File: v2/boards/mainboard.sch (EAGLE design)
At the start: 163 parts, among them IC1 LM2596S-ADJ, IC10 PCF8574P, IC11 UDN2981A, IC13 PAM8403, IC2 LM2596S-5.0, IC3 LD1117A, IC4 LM393, IC5 MCP101-300, IC6 TSOP34830, IC7 DRV8835, IC8 TEENSY 3.6, IC9 PCA9634, J1 Bat_In, J10 SPI_2, J11 I2C_0, J12 I2C_1, J13 I2C_3, J133 USB_Host, J14 BNO055, J15 Uart_2, J16 Uart_5, J17 Uart_6 (LP), J18 BPS, J19 Servo_2, J2 Erw_Pow, J20 Servo_3, J21 Erw_Servo, J22 Erw_PWM, J23 ESP01 Prog, J24 SWD, J25 SWD_KL02, J26 SWD_KL02, J27 SPEAKER_L, J28 SPEAKER_R, J29 AUDIO_TEENSY, J3 Servo_1, J30 Erw_ENA, J31 Erw_GPIO, J32 Erw_analog, J4 H-Bridge Mode, J5 I2C0_5V, J6 SPI_0, J7 SPI_0, J8 SPI_0, J9 SPI_2, SW1 TL32PO, U1 IRL3103, U2 BS108, U3 BS108, U4 BS108, U5 BS108, U6 BS108, U7 BS108, X1 max. 18V

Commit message: ct-bot v2 schematic updated
 - use of i2c sensors
 - adjustable luminosity for CNY70 sensors
 - ENA driver circuit updated for low-side switching
 - ESP32 for Wi-Fi, SWD, RC5 decoding
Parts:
- removed C32: 100nF, rcl:C-EU025-025X050
- removed ESP-12: ESP-12, adafruit:ESP-12
- removed J133: USB_Host, ct-bot:PINHD-1X4
- removed U2, U3: BS108, ct-bot:BS108
- added C29: 470uF, rcl:CPOL-EUE3.5-8
- added D5, D6, D7, D8, D9: 1N4148, ct-bot:1N41480207/2V
- added IC12: ESP-WROOM-32, ct-bot:ESP-WROOM-32
- added J33: Erw_analog, ct-bot:PINHD-1X2
- added J34: USB_Host, ct-bot:PINHD-1X4
- added R53, R54: 4k7, rcl:R-EU_0204/2V
- added R55, R56: 10k, rcl:R-EU_0204/2V
- added R57: 5k, ct-bot:R-TRIMM64W
- added R58: ?, rcl:R-EU_0204/2V
- added R59: ?, rcl:R-EU_0204/7
- added U8, U9: BS108, ct-bot:BS108
- C17: value 220uF -> 100nF; device rcl:CPOL-EUE2-5 -> rcl:C-EU025-025X050
- C18: value 100nF -> 220uF; device rcl:C-EU025-025X050 -> rcl:CPOL-EUE2-5
- C20: value 100uF -> 100nF; device rcl:CPOL-EUE2-5 -> rcl:C-EU025-025X050
- C22: value 470nF -> 10uF
- C23, C27: value 1uF -> 470nF
- C25: value 100nF -> 1uF
- C26: value 470nF -> 100nF
- C28: value 470uF -> 1uF; device rcl:CPOL-EUE3.5-8 -> rcl:C-EU025-025X050
- IC10: value PCF8574P -> TSOP34830; device ct-bot:PCF8574P -> ct-bot:TSOP34830
- IC11: value UDN2981A -> DRV8835; device ct-bot:UDN2981A -> ct-bot:DRV8835THROUGHHOLE
- IC6: value TSOP34830 -> TEENSY 3.6; device ct-bot:TSOP34830 -> ct-bot:TEENSY3_6
- IC7: value DRV8835 -> PCA9634; device ct-bot:DRV8835THROUGHHOLE -> ct-bot:PCA9634-SO20
- IC8: value TEENSY 3.6 -> PCA9672; device ct-bot:TEENSY3_6 -> ct-bot:PCA9672D
- J10, J9: value SPI_2 -> SPI_0
- J11: value I2C_0 -> SPI_2; device ct-bot:PINHD-1X4 -> ct-bot:PINHD-1X7
- J12: value I2C_1 -> SPI_2; device ct-bot:PINHD-1X4 -> ct-bot:PINHD-1X6
- J13: value I2C_3 -> I2C_0
- J14: value BNO055 -> I2C_1; device ct-bot:PINHD-1X6 -> ct-bot:PINHD-1X4
- J15: value Uart_2 -> I2C_3
- J16: value Uart_5 -> BNO055; device ct-bot:PINHD-1X4 -> ct-bot:PINHD-1X6
- J17: value Uart_6 (LP) -> Uart_2
- J18: value BPS -> Uart_5; device ct-bot:PINHD-1X3 -> ct-bot:PINHD-1X4
- J19: value Servo_2 -> Uart_6 (LP)
- J20: value Servo_3 -> BPS; device ct-bot:PINHD-1X4 -> ct-bot:PINHD-1X3
- J21: value Erw_Servo -> Servo_2; device ct-bot:PINHD-1X2 -> ct-bot:PINHD-1X4
- J22: value Erw_PWM -> Servo_3; device ct-bot:PINHD-1X6 -> ct-bot:PINHD-1X4
- J23: value ESP01 Prog -> Erw_Servo; device ct-bot:PINHD-1X4 -> ct-bot:PINHD-1X2
- J24: value SWD -> Erw_PWM
- J25: value SWD_KL02 -> ESP32_PROG; device ct-bot:PINHD90-1X2/90 -> ct-bot:PINHD-1X3
- J26: value SWD_KL02 -> SPEAKER_L
- J27: value SPEAKER_L -> SPEAKER_R
- J28: value SPEAKER_R -> AUDIO_TEENSY; device ct-bot:PINHD-1X2 -> ct-bot:PINHD-1X3
- J29: value AUDIO_TEENSY -> SWD; device ct-bot:PINHD-1X3 -> ct-bot:PINHD-1X6
- J3: value Servo_1 -> I2C0_5V
- J30: value Erw_ENA -> SWD_KL02; device pinhead:PINHD-2X4 -> ct-bot:PINHD90-1X2/90
- J31: value Erw_GPIO -> Erw_ENA; device ct-bot:PINHD-1X2 -> ct-bot:PINHD-1X3
- J32: value Erw_analog -> Erw_GPIO
- J4: value H-Bridge Mode -> I2C3_5V; device ct-bot:PINHD-1X2 -> ct-bot:PINHD-1X4
- J5: value I2C0_5V -> Servo_1
- J6: value SPI_0 -> H-Bridge Mode; device con-harting-ml:ML10 -> ct-bot:PINHD-1X2
- J7: value SPI_0 -> RC5_SEL; device ct-bot:PINHD-1X7 -> ct-bot:PINHD-1X3
- J8: device ct-bot:PINHD-1X6 -> con-harting-ml:ML10
- LDR1, LDR2: value MPY54C569 -> (none)
- R10, R11: value 47k -> 180
- R12, R13: value 210 -> 47k
- R27, R28, R29, R30, R31: device rcl:R-EU_0204/2V -> rcl:R-EU_0204/7
- R32: value 470k -> 100
- R34: value 4k7 -> 470k
- R35: value 100 -> 4k7
- R37: value 3k9 -> 10k
- R38: value 220 -> 10k
- R39: value 590 -> 1k1
- R40: value 115 -> 1k1
- R42, R48: value 4k7 -> 1k8
- R44: value 4k7 -> 3k9
- R45: value 4k7 -> 220
- R46: value 10k -> 590
- R47: value 10k -> 115
- R50: value 5k -> 4k7; device ct-bot:R-TRIMM64W -> rcl:R-EU_0204/2V
- R51: value ? -> 10k
- R52: value ? -> 4k7
- ST3: device ct-bot:PS25-5PS25-5 -> ct-bot:PS25-6
- U1: device transistor-power:IRF740 -> ct-bot:IRF740
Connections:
- removed net ABST_SHUT_L: IC10.P3, U2.G
- removed net ABST_SHUT_R: IC10.P4, U3.G
- removed net DRV_ERW_3: IC11.O7, J30.6
- removed net DRV_ERW_4: IC11.O8, J30.8
- removed net DRV_KANTLED: IC11.O2, R14.2, R15.1
- removed net DRV_LINIE: IC11.O3, R18.2, R19.2
- removed net DRV_RADLED: IC11.O1, R12.2, R13.1
- removed net DRV_SCHRANKE: IC11.O4, ST1.9
- removed net ENA_ERW_2: IC10.P7, IC11.I6, J30.3
- removed net ENA_ERW_3: IC11.I8, J30.5
- removed net ENA_ERW_4: IC11.I7, J30.7
- removed net ENA_KANTLED: IC10.P1, IC11.I2
- removed net ENA_LINIE: IC10.P2, IC11.I3
- removed net ENA_RADLED: IC10.P0, IC11.I1
- removed net ENA_SCHRANKE: IC10.P5, IC11.I4
- removed net N$12: ESP-12.GPIO15, J23.3
- removed net N$14: ESP-12.GPIO0, J23.2
- new net ABST_SHDN_L: D5.C, IC8.P0
- new net ABST_SHDN_R: D6.C, IC8.P1
- new net BNO055_RESET: IC8.P3, J16.6
- new net DRV_KANTLED_L: IC9.LED2, R11.2
- new net DRV_KANTLED_R: IC9.LED3, R15.1
- new net DRV_LINE_L: IC9.LED4, R19.2
- new net DRV_LINE_R: IC9.LED5, R18.2
- new net DRV_RADLED_L: IC9.LED0, R10.2
- new net DRV_RADLED_R: IC9.LED1, R14.1
- new net EN: D8.A, IC12.EN, R56.1
- new net ENA_AUDIO: IC13.SHND, IC8.P4
- new net ESP32_PROG: D9.C, IC8.P6
- new net ESP32_RESET: D8.C, IC8.P5
- new net GPIO_28: IC6.28/ALT-MOSI0, J7.3
- new net IO0: D9.A, IC12.IO0, R55.2
- new net IO10: IC12.SD3
- new net IO11: IC12.CMD
- new net IO13: IC12.IO13
- new net IO15: IC12.IO15
- new net IO18: IC12.IO18
- new net IO19: IC12.IO19
- new net IO21: IC12.IO21
- new net IO34: IC12.IO34
- new net IO35: IC12.IO35
- new net IO36: IC12.SENSOR_VP
- new net IO39: IC12.SENSOR_VN
- new net IO4: IC12.IO4
- new net IO5: IC12.IO5
- new net IO6: IC12.CLK
- new net IO7: IC12.SDO
- new net IO8: IC12.SD1
- new net IO9: IC12.SD2
- new net N$49: IC8.!RESET, R51.1
- new net RC5_ESP32: IC12.IO23, J7.1
- new net RXD0: IC12.RXD0, J25.3
- new net SCHRANKE_SHDN: D7.C, IC8.P2
- new net SCL3_5V: IC7.SCL, IC8.SCL, IC9.SCL, J4.4, R42.1, U8.D
- new net SDA3_5V: IC7.SDA, IC8.SDA, IC9.SDA, J4.3, R41.1, U9.D
- new net TXD0: IC12.TXD0, J25.2
- new net VL6180X_SHDN: D7.A, ST1.5
- net +3V3: now also C22.1, IC10.VS, IC12.3V3, J20.3, J8.10, R12.2, R13.1, R36.2, R39.2, R40.2, R52.2, R53.2, R54.2, R55.1, R56.2, U8.G, U9.G; no longer C21.1, ESP-12.CH_PD, ESP-12.VCC, IC6.VS, J18.3, J23.1, J6.10, R10.2, R11.1, R44.2, R45.2, R48.2, R49.2
- net +5V: now also C17.1, C18.+, C20.1, C21.1, C25.1, C28.1, C29.+, IC11.VCC, IC6.VIN, IC7.A0, IC7.A2, IC7.A4, IC7.VDD, IC8.VDD, IC9.A3, J10.1, J14.2, J16.1, J18.2, J19.2, J3.2, J34.1, J4.2, J9.1, R37.2, R38.2, R41.2, R42.2, R44.1, R45.1, R46.1, R47.1, R48.1, R49.1, R50.1, R51.2, ST1.1, ST2.1, ST3.1; no longer C16.1, C17.+, C18.1, C20.+, C23.1, C27.1, C28.+, IC10.A0, IC10.VDD, IC11.VS, IC7.VCC, IC8.VIN, J10.2, J133.1, J14.1, J16.2, J4.1, J5.2, J7.1, J9.2, R36.1, R37.1, R38.1, R39.1, R40.1, R41.1, R42.1, R46.2, R47.2, ST1.3, ST2.3
- net +6V: now also IC11.VIN, J21.2, J22.2, J5.2; no longer IC7.VIN, J19.2, J20.2, J3.2
- net 3V3_TEENSY: now also C16.1, IC6.3V3, J29.1; no longer C32.1, IC8.3V3, J24.1
- net A22_DAC1: now also IC6.DAC1, J33.1; no longer IC8.DAC1, J32.1
- net AUDIO_OUT: now also IC6.DAC0, J28.1, J33.2; no longer IC8.DAC0, J29.1, J32.2
- net BAT_IN_FB: now also IC6.39/A20/ALT-MISO0; no longer IC8.39/A20/ALT-MISO0
- net BPS: now also IC6.42, J20.1; no longer IC8.42, J18.1
- net DRV_ERW_1: now also IC9.LED6, J31.2; no longer IC11.O5, J30.2
- net DRV_ERW_2: now also IC9.LED7, J31.3; no longer IC11.O6, J30.4
- net ENA_ERW_1: now also IC8.P7, J31.1; no longer IC10.P6, IC11.I5, J30.1
- net ENC_L: now also ST1.8; no longer ST1.1
- net ENC_R: now also ST2.8; no longer ST2.1
- net FERNBED: now also IC10.OUT, J7.2; no longer IC6.OUT, IC8.28/ALT-MOSI0
- net GND: now also C17.2, C18.-, C20.2, C22.2, C26.2, C28.2, C29.-, IC10.GND, IC11.LGND, IC11.MGND, IC12.GND@1, IC12.GND@15, IC12.GND@38, IC12.IO2, IC6.AGND, IC7.A1, IC7.A3, IC7.A5, IC7.A6, IC7.OE, IC7.VSS, IC8.AD0, IC8.AD1, IC8.VSS, J10.2, J14.1, J16.3, J18.1, J20.2, J21.1, J22.1, J25.1, J29.3, J34.4, J4.1, J9.2, R57.E, ST3.6; no longer C17.-, C18.2, C20.-, C23.2, C27.2, C28.-, C32.2, ESP-12.GND, IC10.A1, IC10.A2, IC10.VSS, IC11.GND, IC7.LGND, IC7.MGND, IC8.AGND, IC8.GND, IC9.A3, J10.1, J133.4, J14.3, J16.1, J18.2, J20.1, J23.4, J24.3, J6.2, J7.2, J9.1, R50.E, ST3.5, U2.S, U3.S
- net GPIO_24: now also IC6.24, J32.1; no longer IC8.24, J31.1
- net GPIO_46: now also IC6.46/SCK2, J32.2; no longer IC8.46/SCK2, J31.2
- net KANTE_L: now also IC6.18/A4/PWM/T/SDA0, R12.1, ST1.9; no longer IC8.18/A4/PWM/T/SDA0, R10.1, ST1.6
- net KANTE_R: now also IC6.19/A5/PWM/T/SCL0, R13.2, ST2.9; no longer IC8.19/A5/PWM/T/SCL0, R11.2, ST2.6
- net KL02_DC: now also IC12.IO12, J30.1; no longer J25.1, J26.1
- net KL02_DD: now also IC12.IO14, J30.2; no longer J25.2, J26.2
- net LDR_L: now also IC6.49/A23, R33.1; no longer IC8.49/A23, R32.1
- net LDR_R: now also IC6.50/A24, R34.1; no longer IC8.50/A24, R33.1
- net LINE_IN_L: now also J28.2, R57.A; no longer J29.2, R50.A
- net LINE_IN_R: now also C27.2, J28.3; no longer C26.2, J29.3
- net LINIE_L: now also IC6.A10, ST3.4; no longer IC8.A10, ST3.3
- net LINIE_R: now also IC6.A11, ST3.5; no longer IC8.A11, ST3.4
- net MOT_L_1: now also IC11.AOUT1; no longer IC7.AOUT1
- net MOT_L_2: now also IC11.AOUT2; no longer IC7.AOUT2
- net MOT_L_DIR: now also IC11.APHASE, IC6.40; no longer IC7.APHASE, IC8.40
- net MOT_L_PWM: now also IC11.AENBL, IC6.35/A16/PWM; no longer IC7.AENBL, IC8.35/A16/PWM
- net MOT_R_1: now also IC11.BOUT1; no longer IC7.BOUT1
- net MOT_R_2: now also IC11.BOUT2; no longer IC7.BOUT2
- net MOT_R_DIR: now also IC11.BPHASE, IC6.41; no longer IC7.BPHASE, IC8.41
- net MOT_R_PWM: now also IC11.BENBL, IC6.36/A17/PWM; no longer IC7.BENBL, IC8.36/A17/PWM
- net N$1: now also ST3.3; no longer ST3.2
- net N$13: now also IC7.LED2; no longer IC9.LED2
- net N$15: now also IC7.LED3; no longer IC9.LED3
- net N$16: now also IC7.LED4; no longer IC9.LED4
- net N$17: now also IC7.LED5; no longer IC9.LED5
- net N$18: now also IC7.LED6; no longer IC9.LED6
- net N$19: now also IC7.LED7; no longer IC9.LED7
- net N$20: now also R43.2; no longer R36.2
- net N$21: now also R44.2; no longer R37.2
- net N$22: now also R45.2; no longer R38.2
- net N$23: now also R46.2; no longer R39.2
- net N$24: now also R47.2; no longer R40.2
- net N$25: now also R48.2; no longer R41.2
- net N$26: now also R49.2; no longer R42.2
- net N$27: now also R50.2; no longer R43.2
- net N$28: now also R32.1; no longer R35.1
- net N$3: now also IC11.MODE, J6.2; no longer IC7.MODE, J4.2
- net N$30: now also ST3.2; no longer ST3.1
- net N$31: now also J26.2; no longer J27.2
- net N$32: now also J26.1; no longer J27.1
- net N$33: now also C26.1; no longer C25.1
- net N$40: now also R58.1; no longer R51.1
- net N$41: now also C23.1, R58.2; no longer C22.1, R51.2
- net N$42: now also C23.2, R57.S; no longer C22.2, R50.S
- net N$43: now also J27.1; no longer J28.1
- net N$44: now also J27.2; no longer J28.2
- net N$45: now also R14.2, ST2.6; no longer R13.2, ST2.2
- net N$46: now also R59.1; no longer R52.1
- net N$47: now also R10.1, ST1.6; no longer R12.1, ST1.2
- net N$48: now also C27.1, R59.2; no longer C26.1, R52.2
- net N$51: now also R11.1, ST1.7; no longer R14.1, ST1.5
- net N$53: now also ST2.7; no longer ST2.5
- net N$6: now also IC7.LED0; no longer IC9.LED0
- net N$7: now also IC7.LED1; no longer IC9.LED1
- net PWM_ERW_1: now also IC6.16/A2/PWM/T/ALT-SCL0, J24.1; no longer IC8.16/A2/PWM/T/ALT-SCL0, J22.1
- net PWM_ERW_2: now also IC6.17/A3/PWM/T/ALT-SDA0, J24.2; no longer IC8.17/A3/PWM/T/ALT-SDA0, J22.2
- net PWM_ERW_3: now also IC6.30/PWM/T/ALT-CAN0RX, J24.3, J8.9; no longer IC8.30/PWM/T/ALT-CAN0RX, J22.3, J6.9
- net PWM_ERW_4: now also IC6.29/PWM/T/ALT-CAN0TX, J24.4; no longer IC8.29/PWM/T/ALT-CAN0TX, J22.4
- net PWM_ERW_5: now also IC6.4/PWM/SDA2/CAN0RX, J24.5; no longer IC8.4/PWM/SDA2/CAN0RX, J22.5
- net PWM_ERW_6: now also IC6.3/PWM/SCL2/CAN0TX, J24.6; no longer IC8.3/PWM/SCL2/CAN0TX, J22.6
- net RAD_L: now also IC6.43/CS2-0; no longer IC8.43/CS2-0
- net RAD_R: now also IC6.44/MOSI2; no longer IC8.44/MOSI2
- net RESET: now also IC12.IO22, IC6.RESET, J29.2; no longer IC8.RESET, J24.2
- net RX1: now also IC6.27/ALT-RX1/ALT-SCK0; no longer IC8.27/ALT-RX1/ALT-SCK0
- net RX2: now also IC6.9/PWM/RX2/CS0-1, J17.4; no longer IC8.9/PWM/RX2/CS0-1, J15.4
- net RX5: now also IC12.IO17, IC6.34/A15/CAN1RX/RX5/ALT-SDA0, J18.4; no longer ESP-12.TXD, IC8.34/A15/CAN1RX/RX5/ALT-SDA0, J16.4
- net RX6: now also IC6.47/SCL0/RX6, J19.4; no longer IC8.47/SCL0/RX6, J17.4
- net SCL0: now also IC6.7/PWM/RX3/ALT-SCL0/ALT-MOSI0, J13.4, R36.1; no longer IC10.SCL, IC8.7/PWM/RX3/ALT-SCL0/ALT-MOSI0, IC9.SCL, J11.4, R45.1
- net SCL0_5V: now also J16.5, J3.4, R38.1, ST1.3, ST2.3; no longer J14.5, J5.4, R47.1, ST1.8, ST2.8
- net SCL1: now also IC6.37/A18/PWM/SCL1, J14.4; no longer IC8.37/A18/PWM/SCL1, J12.4
- net SCL3: now also IC12.IO26, IC6.57/SCL3/PWM, J15.3, R40.1, U8.S; no longer IC8.57/SCL3/PWM, J13.3
- net SDA0: now also IC6.8/PWM/TX3/ALT-SDA0/ALT-MISO0, J13.3, R35.1; no longer IC10.SDA, IC8.8/PWM/TX3/ALT-SDA0/ALT-MISO0, IC9.SDA, J11.3, R44.1
- net SDA0_5V: now also J16.4, J3.3, R37.1, ST1.2, ST2.2; no longer J14.4, J5.3, R46.1, ST1.7, ST2.7
- net SDA1: now also IC6.38/A19/PWM/SDA1, J14.3; no longer IC8.38/A19/PWM/SDA1, J12.3
- net SDA3: now also IC12.IO25, IC6.56/SDA3/PWM, J15.4, R39.1, U9.S; no longer IC8.56/SDA3/PWM, J13.4
- net SERVO1_FB: now also IC6.22/A8/PWM/T, J5.4; no longer IC8.22/A8/PWM/T, J3.4
- net SERVO1_PWM: now also IC6.5/PWM/ALT-TX1/ALT-MISO1, J5.3, R52.1; no longer IC8.5/PWM/ALT-TX1/ALT-MISO1, J3.3, R34.1
- net SERVO2_FB: now also IC6.23/A9/PWM/T, J21.4; no longer IC8.23/A9/PWM/T, J19.4
- net SERVO2_PWM: now also IC6.6/PWM, J21.3, R53.1; no longer IC8.6/PWM, J19.3, R48.1
- net SERVO3_PWM: now also IC6.25, J22.3, R54.1; no longer IC8.25, J20.3, R49.1
- net SERVO4_PWM: now also IC6.20/A6/PWM/CS0-2/ALT-SCK1, J23.1, J9.6; no longer IC8.20/A6/PWM/CS0-2/ALT-SCK1, J21.1, J7.6
- net SERVO5_PWM: now also IC6.21/A7/PWM/CS0-3/ALT-MOSI1/ALT-RX1, J10.6, J23.2, J9.7; no longer IC8.21/A7/PWM/CS0-3/ALT-MOSI1/ALT-RX1, J21.2, J7.7, J8.6
- net SPI0_CS0: now also IC6.2/PWM, J8.6; no longer IC8.2/PWM, J6.6
- net SPI0_CS4: now also IC6.15/A1/CS0-4/T, J8.7; no longer IC8.15/A1/CS0-4/T, J6.7
- net SPI0_CS5: now also IC6.45/CS0-5/MISO2, J8.8; no longer IC8.45/CS0-5/MISO2, J6.8
- net SPI0_MISO: now also IC6.12/MISO0, J10.4, J9.4; no longer IC8.12/MISO0, J6.4, J7.4
- net SPI0_MOSI: now also IC6.11/MOSI0, J10.3, J9.3; no longer IC8.11/MOSI0, J6.3, J7.3
- net SPI0_SCK: now also IC6.14/A0/PWM/ALT-SCK0, J10.5, J9.5; no longer IC8.14/A0/PWM/ALT-SCK0, J6.5, J7.5
- net SPI1_CS0: now also IC6.31/A12/PWM/RX4/CS1-0; no longer IC8.31/A12/PWM/RX4/CS1-0
- net SPI1_MISO: now also IC6.1/TX1/MISO1/T; no longer IC8.1/TX1/MISO1/T
- net SPI1_MOSI: now also IC6.0/RX1/MOSI1/T; no longer IC8.0/RX1/MOSI1/T
- net SPI1_SCK: now also IC6.32/A13/PWM/TX4/SCK1; no longer IC8.32/A13/PWM/TX4/SCK1
- net SPI2_CS0: now also IC6.55, J11.6; no longer IC8.55, J9.6
- net SPI2_CS1: now also IC6.54/CS2-1, J11.7, J12.6; no longer IC8.54/CS2-1, J10.6, J9.7
- net SPI2_MISO: now also IC6.51/MISO2, J11.4, J12.4; no longer IC8.51/MISO2, J10.4, J9.4
- net SPI2_MOSI: now also IC6.52/MOSI2, J11.3, J12.3; no longer IC8.52/MOSI2, J10.3, J9.3
- net SPI2_SCK: now also IC6.53/PWM/SCK2, J11.5, J12.5; no longer IC8.53/PWM/SCK2, J10.5, J9.5
- net SWCLK: now also IC12.IO33, IC6.DC, J29.5; no longer IC8.DC, J24.5
- net SWDIO: now also IC12.IO32, IC6.DD, J29.6; no longer IC8.DD, J24.6
- net SWD_EN: now also IC12.IO27, IC6.DE, J29.4; no longer IC8.DE, J24.4
- net TEENSY_LED: now also IC6.13/LED/ALT-PWM/SCK0; no longer IC8.13/LED/ALT-PWM/SCK0
- net TX1: now also IC6.26/ALT-PWM/ALT-TX1/ALT-SCL2; no longer IC8.26/ALT-PWM/ALT-TX1/ALT-SCL2
- net TX2: now also IC6.10/PWM/TX2/CS0-0, J17.3; no longer IC8.10/PWM/TX2/CS0-0, J15.3
- net TX5: now also IC12.IO16, IC6.33/A14/CAN1TX/TX5/ALT-SCL0, J18.3; no longer ESP-12.RXD, IC8.33/A14/CAN1TX/TX5/ALT-SCL0, J16.3
- net TX6: now also IC6.48/SDA0/TX6, J19.3; no longer IC8.48/SDA0/TX6, J17.3
- net USB1_D+: now also IC6.D+, J34.3; no longer IC8.D+, J133.3
- net USB1_D-: now also IC6.D-, J34.2; no longer IC8.D-, J133.2
- net VBAT_RTC: now also IC6.VBAT; no longer IC8.VBAT
- net VL53L0X_SHUT_L: now also D5.A; no longer U2.D
- net VL53L0X_SHUT_R: now also D6.A; no longer U3.D
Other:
- note added: "Aktuatoren"
- note added: "ENA PWM"
- note added: "ENA digital"
- note added: "LDRs"
- note added: "LEDs"
- note added: "Power"
- note added: "RC5"
- note added: "Radencoder"
- note added: "Rev. 0.8.0"
- note added: "Sensoren"
- note added: "Teensy"
- note added: "ToDo: Signalauswahl"
- note added: "ToDo: testen"
- note removed: "/ MIC2981 / TBD62783A"
- note removed: "ESP12"
- note removed: "Rev. 0.7"
- note removed: "TODO: SWD-Pins verbinden an GPIOs? Widerstaende?"
- note removed: "ToDo: alternativ low-side switch (ULN 2803)?"
- note removed: "ToDo: testen! SHDN?"
- moved on the sheet: BT1, C10, C13, C16, C19, C22, C23, C24, C26, C27, IC13, IC5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

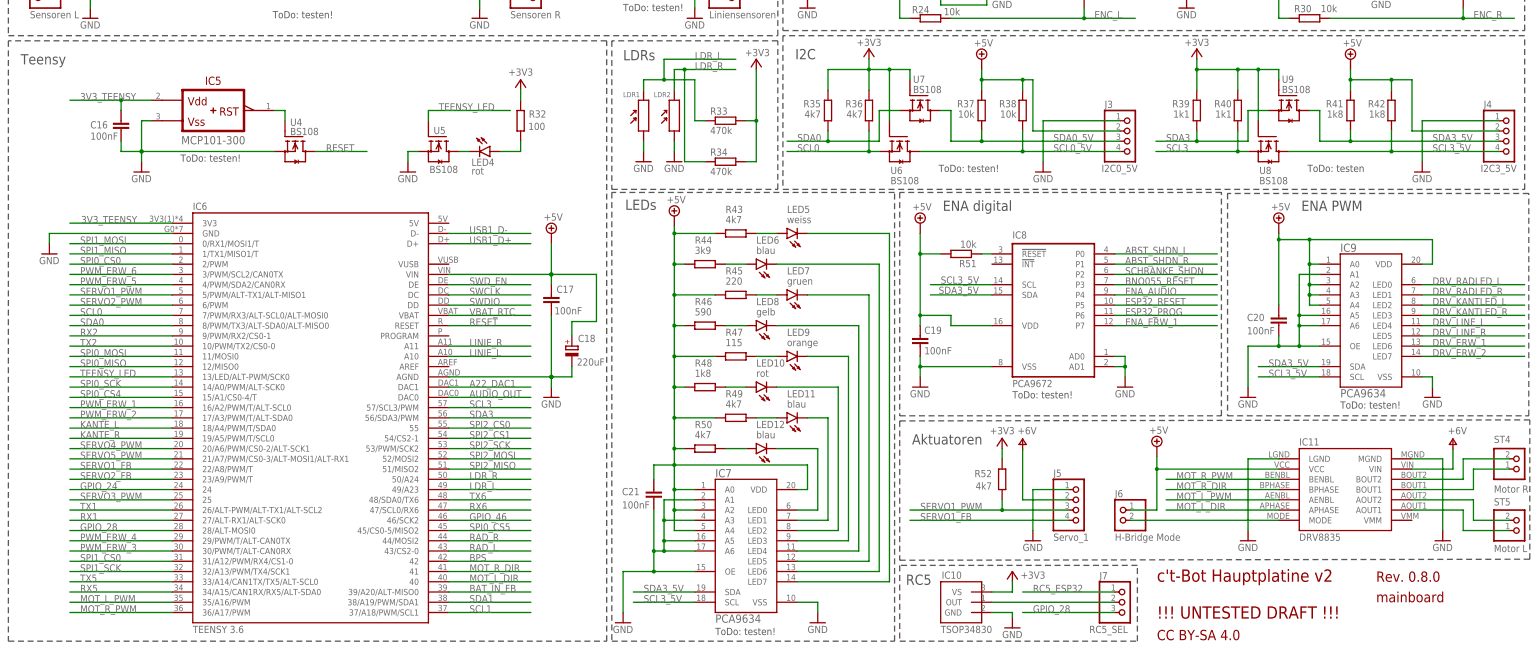
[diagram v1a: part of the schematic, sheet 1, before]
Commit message: PCA9672D (no longer manufactured) replaced with PCA9554D
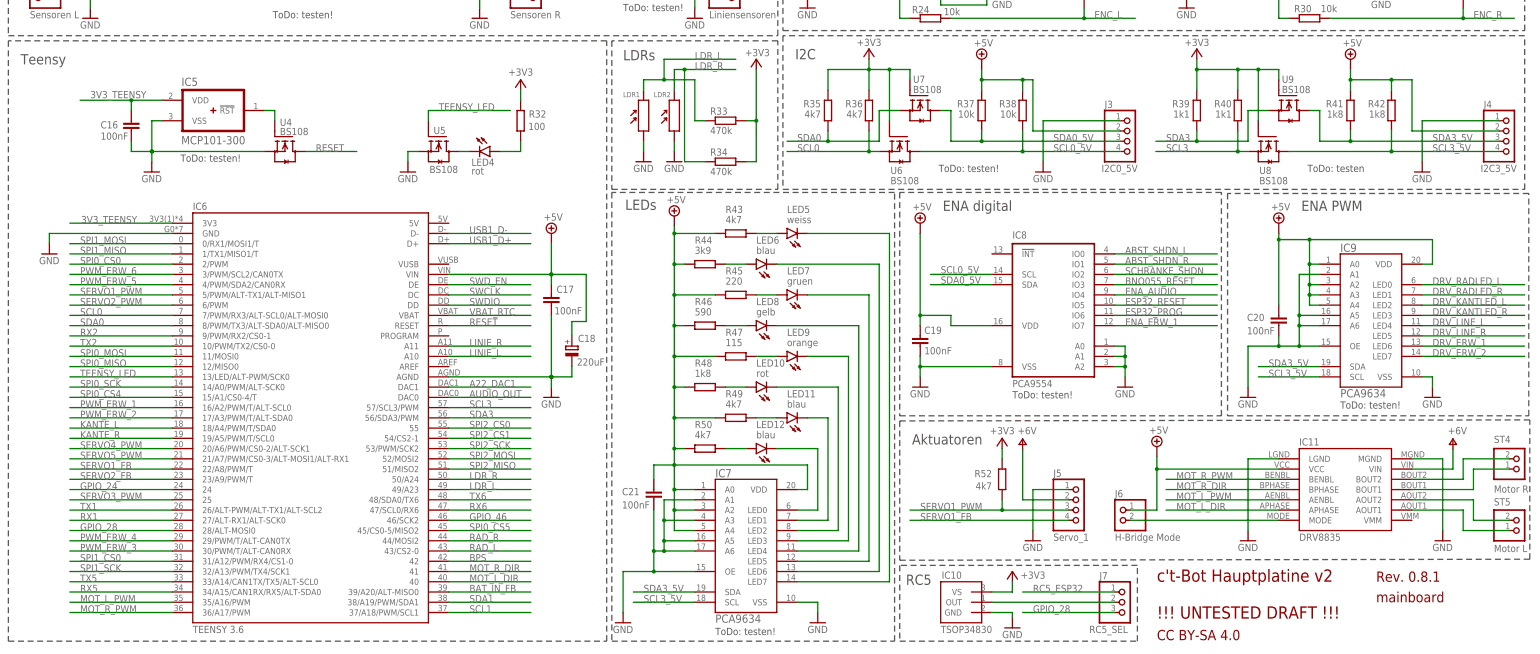
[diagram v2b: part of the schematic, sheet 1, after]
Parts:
- removed R51: 10k, rcl:R-EU_0204/2V
- added J35: ESP32_PROG, ct-bot:PINHD-1X3
- IC8: value PCA9672 -> PCA9554; device ct-bot:PCA9672D -> ct-bot:PCA9554D
- J25: value ESP32_PROG -> ESP32_Uart; SPICEPREFIX (none) -> J
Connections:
- removed net N$49: IC8.!RESET, R51.1
- net +5V: no longer R51.2
- net ABST_SHDN_L: now also IC8.IO0; no longer IC8.P0
- net ABST_SHDN_R: now also IC8.IO1; no longer IC8.P1
- net BNO055_RESET: now also IC8.IO3; no longer IC8.P3
- net ENA_AUDIO: now also IC8.IO4; no longer IC8.P4
- net ENA_ERW_1: now also IC8.IO7; no longer IC8.P7
- net ESP32_PROG: now also IC8.IO6, J35.2; no longer IC8.P6
- net ESP32_RESET: now also IC8.IO5, J35.3; no longer IC8.P5
- net GND: now also IC8.A0, IC8.A1, IC8.A2, J35.1; no longer IC8.AD0, IC8.AD1
- net SCHRANKE_SHDN: now also IC8.IO2; no longer IC8.P2
- net SCL0_5V: now also IC8.SCL
- net SCL3_5V: no longer IC8.SCL
- net SDA0_5V: now also IC8.SDA
- net SDA3_5V: no longer IC8.SDA
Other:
- note added: "Rev. 0.8.1"
- note removed: "Rev. 0.8.0"
- moved on the sheet: C16, D8, J25, R56, U4

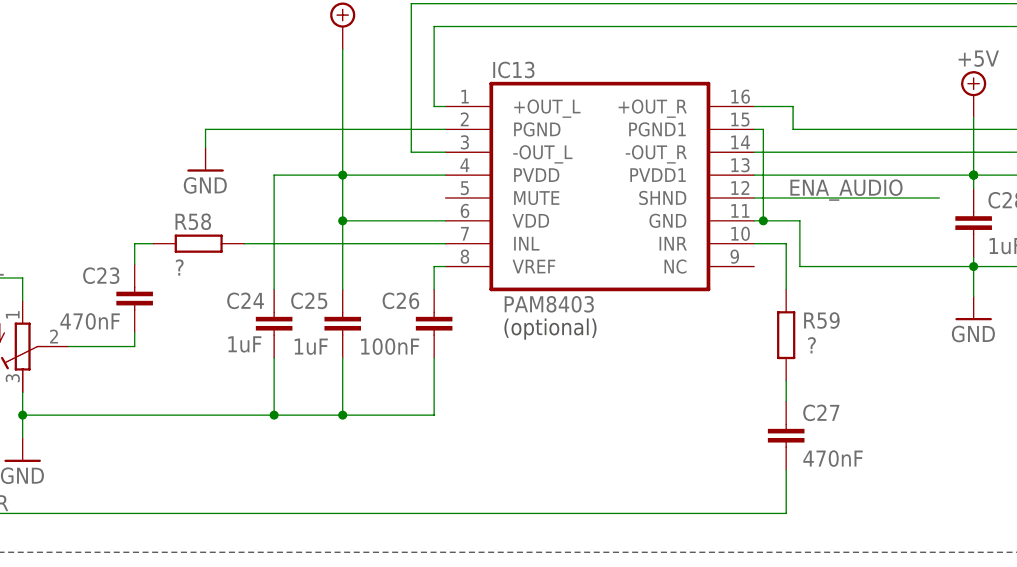
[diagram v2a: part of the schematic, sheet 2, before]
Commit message: resistor values for audio amp updated
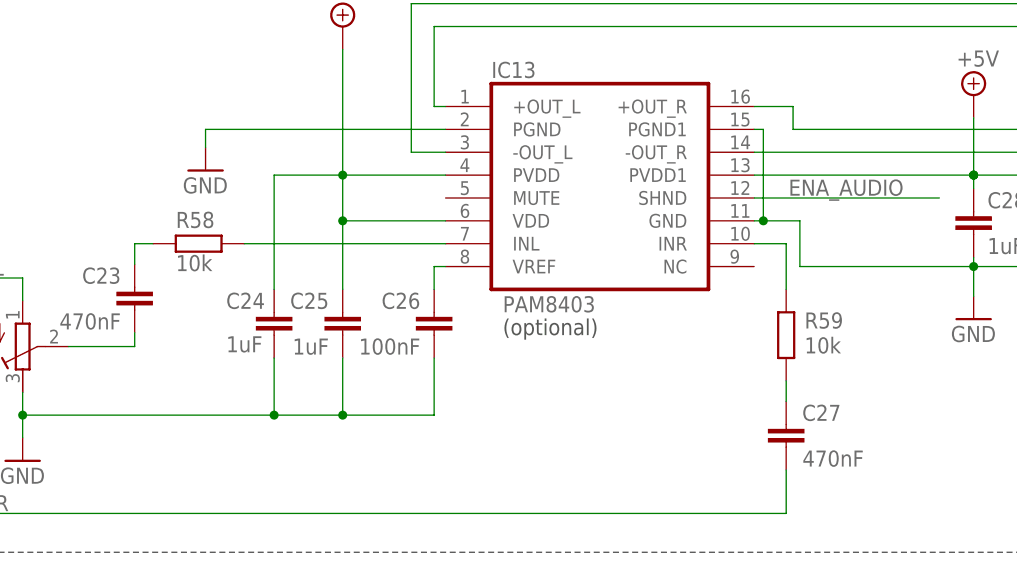
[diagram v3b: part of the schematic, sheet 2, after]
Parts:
- R58, R59: value ? -> 10k
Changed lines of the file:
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@@
 <part name="R32" library="rcl" library_urn="urn:adsk.eagle:library:334" deviceset="R-EU_" device="0204/2V" package3d_urn="urn:adsk.eagle:package:23495/1" value="100"/>
 <part name="+3V7" library="supply1" library_urn="urn:adsk.eagle:library:371" deviceset="+3V3" device=""/>
-<part name="R58" library="rcl" library_urn="urn:adsk.eagle:library:334" deviceset="R-EU_" device="0204/2V" package3d_urn="urn:adsk.eagle:package:23495/1" value="?"/>
+<part name="R58" library="rcl" library_urn="urn:adsk.eagle:library:334" deviceset="R-EU_" device="0204/2V" package3d_urn="urn:adsk.eagle:package:23495/1" value="10k"/>
 <part name="R57" library="ct-bot" deviceset="R-TRIMM" device="64W" package3d_urn="urn:adsk.eagle:package:23748/1" value="5k"/>
 <part name="GND10" library="supply1" library_urn="urn:adsk.eagle:library:371" deviceset="GND" device=""/>
@@
 <part name="C28" library="rcl" library_urn="urn:adsk.eagle:library:334" deviceset="C-EU" device="025-025X050" package3d_urn="urn:adsk.eagle:package:23629/2" value="1uF"/>
 <part name="J27" library="ct-bot" deviceset="PINHD-1X2" device="" value="SPEAKER_R"/>
-<part name="R59" library="rcl" library_urn="urn:adsk.eagle:library:334" deviceset="R-EU_" device="0204/7" package3d_urn="urn:adsk.eagle:package:23498/2" value="?"/>
+<part name="R59" library="rcl" library_urn="urn:adsk.eagle:library:334" deviceset="R-EU_" device="0204/7" package3d_urn="urn:adsk.eagle:package:23498/2" value="10k"/>
 <part name="C27" library="rcl" library_urn="urn:adsk.eagle:library:334" deviceset="C-EU" device="025-025X050" package3d_urn="urn:adsk.eagle:package:23629/2" value="470nF"/>
 <part name="IC7" library="ct-bot" deviceset="PCA9634" device="-SO20" package3d_urn="urn:adsk.eagle:package:30246/1" value="PCA9634"/>
@@
 </instance>
 <instance part="R58" gate="G$1" x="250.698" y="115.57" smashed="yes" rot="R180">
-<attribute name="NAME" x="252.222" y="118.8974" size="1.778" layer="95" rot="R180"/>
-<attribute name="VALUE" x="249.174" y="113.792" size="1.778" layer="96" rot="R180"/>
+<attribute name="NAME" x="248.158" y="117.3226" size="1.778" layer="95"/>
+<attribute name="VALUE" x="248.158" y="112.522" size="1.778" layer="96"/>
 </instance>
 <instance part="R57" gate="G$1" x="231.14" y="104.14" smashed="yes" rot="MR180">
@@
 </instance>
 <instance part="R59" gate="G$1" x="315.976" y="105.41" smashed="yes" rot="R270">
-<attribute name="NAME" x="317.754" y="106.1466" size="1.778" layer="95"/>
-<attribute name="VALUE" x="318.262" y="103.378" size="1.778" layer="96"/>
+<attribute name="NAME" x="318.008" y="106.1466" size="1.778" layer="95"/>
+<attribute name="VALUE" x="318.008" y="103.378" size="1.778" layer="96"/>
 </instance>
 <instance part="C27" gate="G$1" x="315.976" y="95.504" smashed="yes" rot="MR0">
